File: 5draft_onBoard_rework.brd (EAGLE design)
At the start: 93.7 x 72.4 mm, 68 parts, among them IC3 74ABT125PW, IC4 MAX4466KS, J2 USB_MINI-B_DIGIKEY, Q1 NPN 40V 1A SOT-23

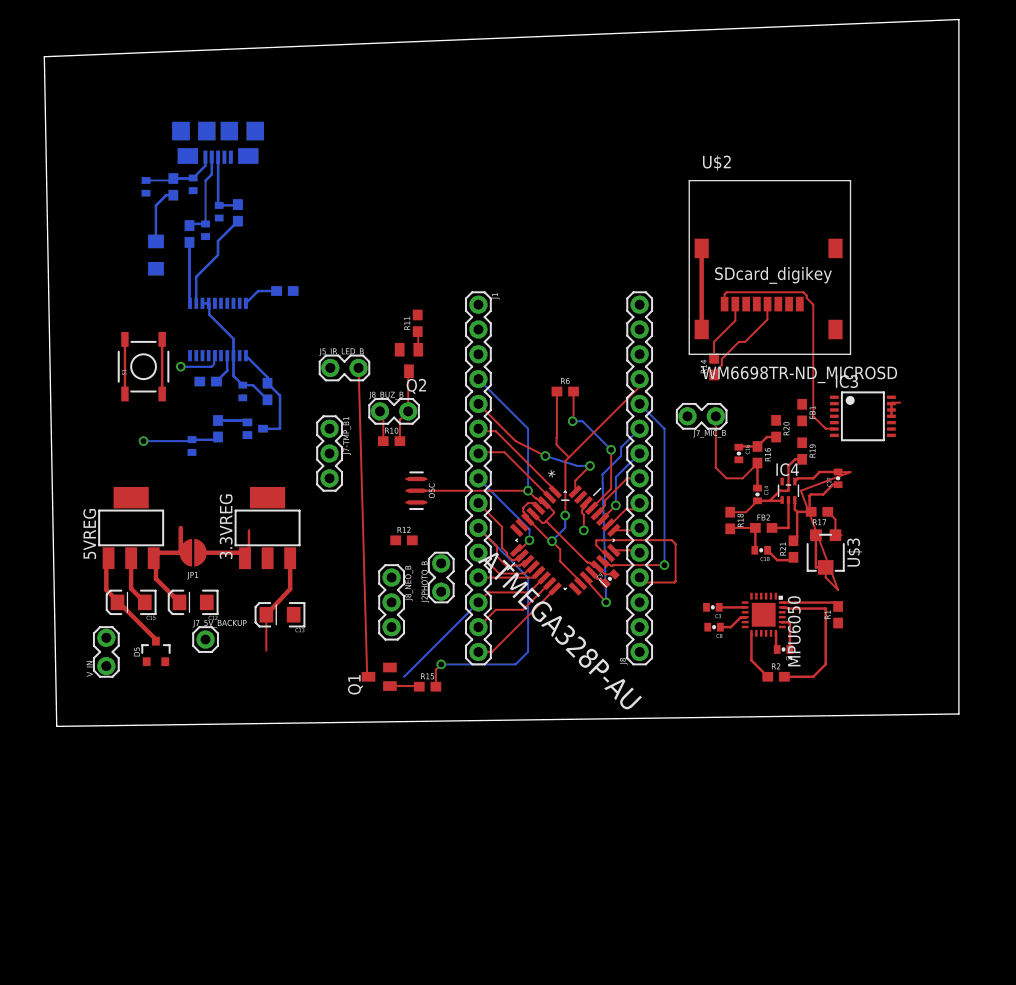
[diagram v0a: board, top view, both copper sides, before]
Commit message: re arranging nano layout
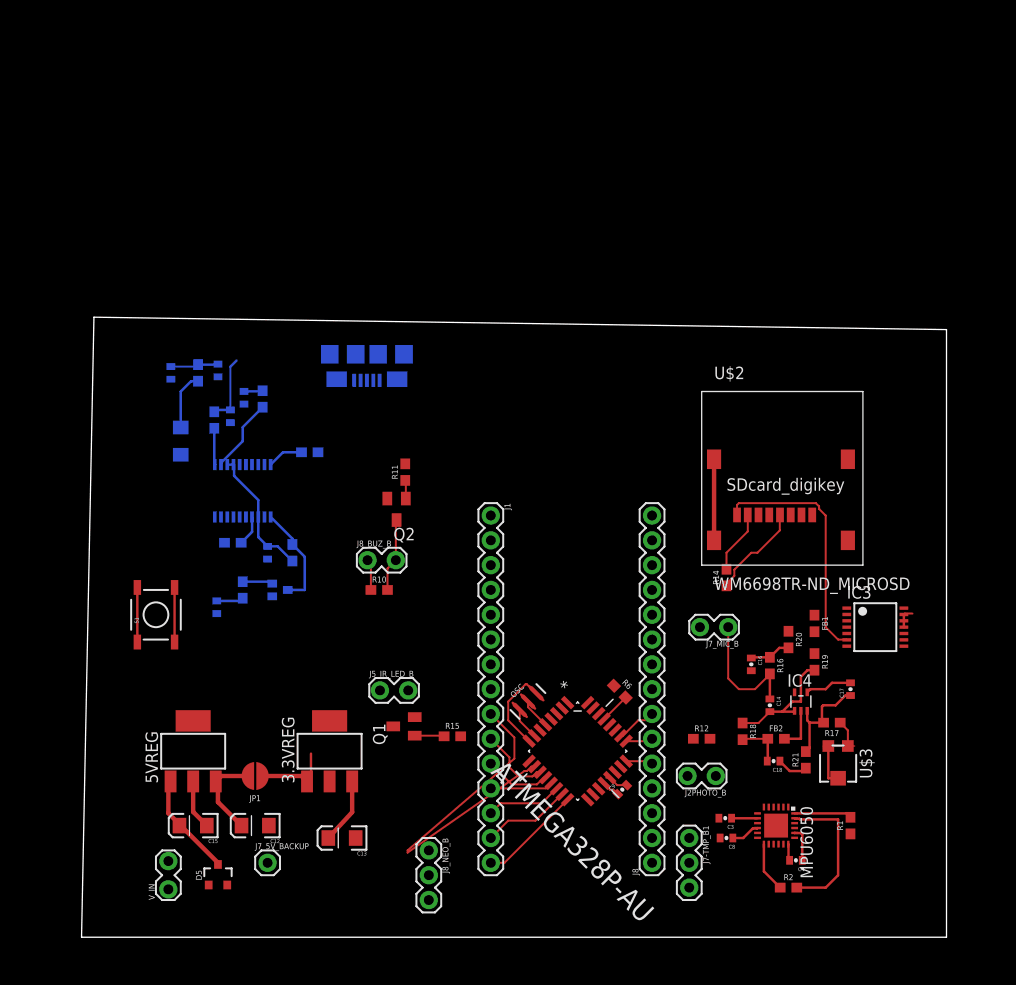
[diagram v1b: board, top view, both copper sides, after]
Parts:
- moved J7-TMP_B1 55.8 mm to (62.2, 6.35)
- moved R12 36.6 mm to (63.5, 16.5)
- moved J2PHOTO_B 33.8 mm to (64.8, 12.7), turned to 180 degrees
- moved J5_IR_LED_B 33.4 mm to (30.7, 21.5)
- moved R6 31.2 mm to (55.1, 21.3), turned to 315 degrees
- moved J8_NEO_B 28.2 mm to (35.6, 5.08)
- moved J2 27.5 mm to (29.2, 55.9)
- moved S1 25.4 mm to (7.62, 29.2)
- moved OSC 24.4 mm to (45.7, 20.3), turned to 45 degrees
- moved J7_5V_BACKUP 23.7 mm to (19.1, 3.81)
- moved JP1 23.7 mm to (17.8, 12.7)
- moved 3.3VREG 23.7 mm to (25.4, 15.2)
- moved 5VREG 23.7 mm to (11.4, 15.2)
- moved C12 23.7 mm to (17.8, 7.62)
- moved C13 23.7 mm to (26.7, 6.35)
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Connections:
- net D+ renamed D+_P
- net D- renamed D-_N
- net N$1 renamed PB6
- net N$14 renamed USBDP_N
- net N$15 renamed USBDM_P
- net N$2 renamed PB7
- net RESET: now also C7.2
- net SDA: no longer C7.2
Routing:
- net A6: track 52.2 -> 9.35 mm, vias 1 -> 0
- net 5V: track 68.9 -> 27.9 mm, vias 2 -> 0
- net GND: track 75.5 -> 35.9 mm, vias 2 -> 0
- net IR_-: track 31.9 -> 0.18 mm
- net D6: track 8.48 -> 36.0 mm
- net D7: track 34.1 -> 7.42 mm, vias 1 -> 0
- net A7: track 24.1 -> 0.00 mm, vias 1 -> 0
- net A0: track 18.3 -> 0.65 mm
- net D2: track 16.8 -> 0.00 mm, vias 2 -> 0
- net RESET: track 15.0 -> 3.12 mm, vias 2 -> 0
- net SS: track 18.5 -> 7.77 mm
- net D3: track 10.8 -> 0.18 mm
- net D5: track 10.3 -> 0.00 mm, vias 1 -> 0
- net D4: track 9.27 -> 0.22 mm
- net PB7: track 0.00 -> 8.94 mm
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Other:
- board size 93.7 x 72.4 mm -> 88.6 x 63.5 mm

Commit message: removed 3.3v and changed buffer to be 5v
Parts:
- removed 3.3VREG: (no value), linear-technology:SOT223
- removed C13: 10uF, SparkFun-Retired:EIA3216
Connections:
- removed net 3.3V: 3.3VREG.3, C13.A, IC3.11, IC3.12, IC3.13, R14.1, U$2.VDD
- net 5V: now also IC3.11, IC3.12, IC3.13, R14.1, U$2.VDD; no longer 3.3VREG.1
- net GND: no longer 3.3VREG.2, 3.3VREG.4, C13.C
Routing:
- net 3.3V: track 18.9 -> 0.00 mm
- net 5V: track 27.9 -> 36.2 mm

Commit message: adding pir sensors to board
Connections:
- removed net USBDP_N: FTDI231XS1.11, R7.2
- new net N$1: FTDI231XS1.12, R7.2
- net USBDM_P: now also FTDI231XS1.11; no longer FTDI231XS1.12
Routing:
- net USBDP_N: track 3.74 -> 0.00 mm
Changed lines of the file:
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@@
 <wire x1="15.87" y1="55.24" x2="28.57" y2="53.21" width="0" layer="19" extent="16-16"/>
-</signal>
-<signal name="USBDP_N">
-<contactref element="R7" pad="2"/>
-<contactref element="FTDI231XS1" pad="11"/>
-<wire x1="13.589" y1="48.299" x2="13.589" y2="44.6532" width="0.254" layer="16"/>
-<wire x1="13.589" y1="44.6532" x2="13.6525" y2="44.5897" width="0.254" layer="16"/>
 </signal>
 <signal name="USBDM_P">
 <contactref element="R5" pad="2"/>
-<contactref element="FTDI231XS1" pad="12"/>
-<wire x1="14.2875" y1="44.5897" x2="14.2875" y2="44.7675" width="0.254" layer="16"/>
 <wire x1="14.2875" y1="44.7675" x2="16.51" y2="46.99" width="0.254" layer="16"/>
 <wire x1="16.51" y1="46.99" x2="16.51" y2="48.426" width="0.254" layer="16"/>
 <wire x1="16.51" y1="48.426" x2="18.542" y2="50.458" width="0.254" layer="16"/>
+<contactref element="FTDI231XS1" pad="11"/>
+<wire x1="13.6525" y1="44.5897" x2="14.2875" y2="44.7675" width="0" layer="19" extent="16-16"/>
 </signal>
 <signal name="RX">
@@
 <wire x1="73.01" y1="21.27" x2="75.057" y2="25.234" width="0" layer="19" extent="1-1"/>
 </signal>
+<signal name="N$1">
+<contactref element="R7" pad="2"/>
+<contactref element="FTDI231XS1" pad="12"/>
+<wire x1="14.2875" y1="44.5897" x2="13.589" y2="48.299" width="0" layer="19" extent="16-16"/>
+</signal>
 </signals>

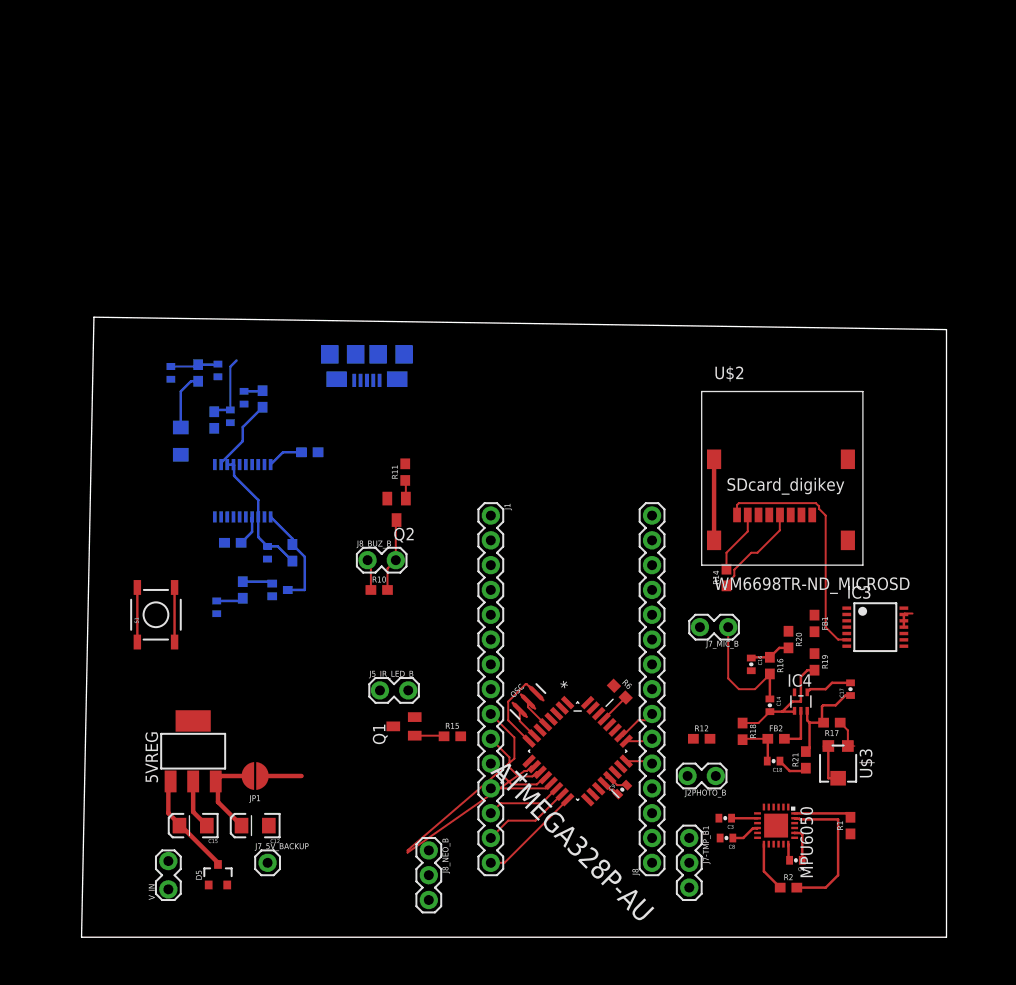
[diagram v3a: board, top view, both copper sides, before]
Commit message: redoing layout, condensing.
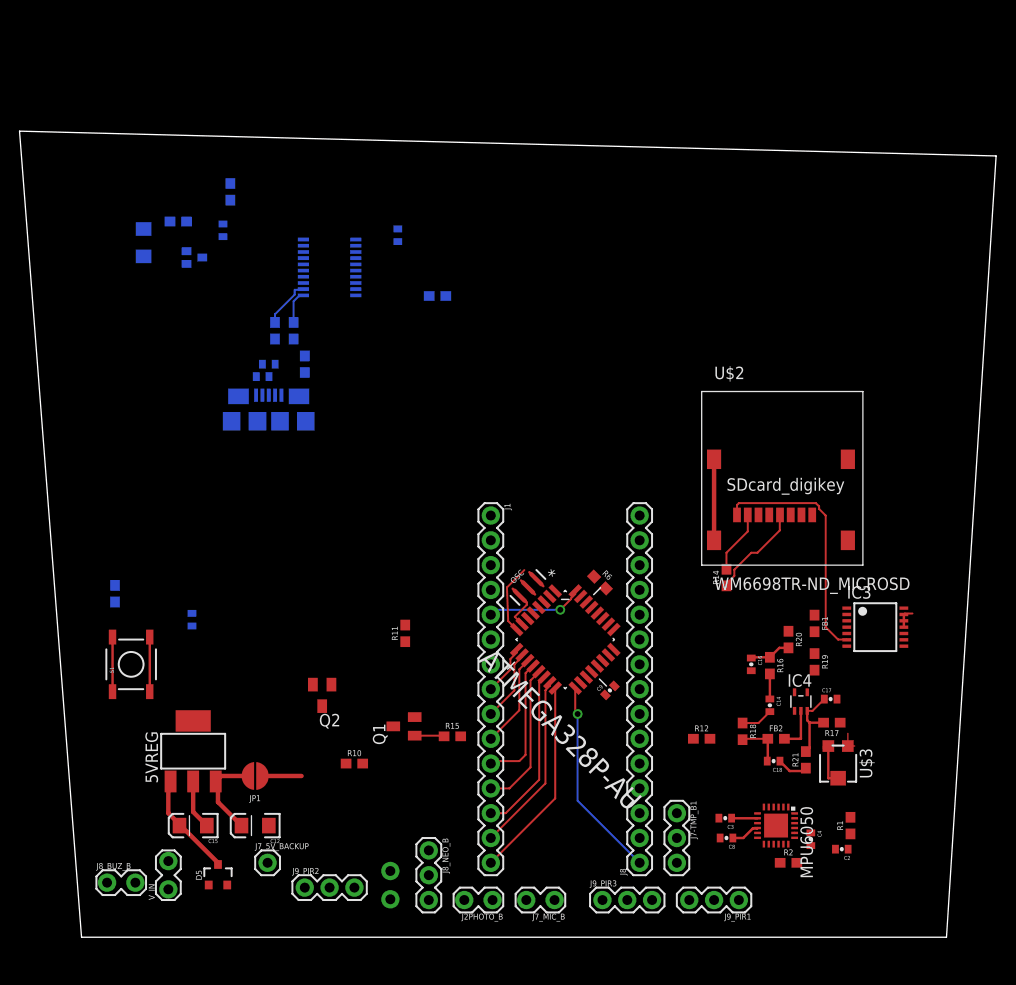
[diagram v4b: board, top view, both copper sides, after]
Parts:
- added J9_PIR1, J9_PIR2, J9_PIR3: (no value), SparkFun-Connectors:1X03
- moved C2 84.3 mm to (77.9, 5.21), flipped to the top, turned to 180 degrees
- moved J8_BUZ_B 42.4 mm to (2.79, 1.78)
- moved R3 35.9 mm to (9.91, 69.5), turned to 0 degrees
- moved U$1 35.1 mm to (11.6, 65.8)
- moved C1 35.1 mm to (32.4, 68.1)
- moved J7_MIC_B 33.1 mm to (48.3, 0.00)
- moved R9 32.8 mm to (36.4, 61.8), turned to 180 degrees
- moved R8 27.9 mm to (15.2, 72.5), turned to 90 degrees
- moved J2PHOTO_B 26.2 mm to (41.9, 0.00)
- moved FTDI231XS1 24.5 mm to (25.4, 64.8), turned to 270 degrees
- moved J5_IR_LED_B 21.2 mm to (31.6, 0.25), flipped to the bottom, turned to 90 degrees
- moved C11 20.7 mm to (6.35, 67.3), turned to 270 degrees
- moved Q2 20.5 mm to (24.6, 21.0)
- moved R10 18.0 mm to (27.9, 14.0)
- moved R11 16.5 mm to (33.1, 27.3)
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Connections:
- net N$1 renamed USBDM_N
- new net VUSB: C11.A, C5.1, FB3.1, FB3.2, FTDI231XS1.15, J2.VCC
- net 5V: now also J9_PIR1.2, J9_PIR2.2, J9_PIR3.2; no longer C11.A, C5.1, FB3.1, FB3.2, FTDI231XS1.15, J2.VCC
- net D4: now also J9_PIR2.1
- net D7: now also J9_PIR1.1
- net D8: now also J9_PIR3.1
- net GND: now also J9_PIR1.3, J9_PIR2.3, J9_PIR3.3
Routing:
- net D6: track 36.0 -> 7.37 mm
- net SCK: track 0.00 -> 20.6 mm, vias 0 -> 1
- net 5V: track 36.2 -> 15.6 mm
- net SCL: track 15.0 -> 0.00 mm
- net 3.3VFTDI: track 13.6 -> 0.00 mm
- net DTR_FTDI: track 10.7 -> 0.00 mm
- net N$24: track 13.2 -> 2.60 mm
- net MISO: track 17.0 -> 27.1 mm
- net D2: track 0.00 -> 9.88 mm, vias 0 -> 1
- net SS: track 7.77 -> 17.1 mm
- net MOSI: track 9.16 -> 18.4 mm
- net N$25: track 12.6 -> 3.53 mm
- net D9: track 6.39 -> 15.1 mm
- net BUZ-: track 7.54 -> 0.00 mm
- net GND: track 35.9 -> 28.5 mm
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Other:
- board size 88.6 x 63.5 mm -> 100 x 82.5 mm
